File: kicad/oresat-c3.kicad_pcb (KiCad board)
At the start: 4 copper layers, 99.8 x 94.6 mm, 564 parts, among them J1 TFM-120-01-L-D-RA, J2 2-1734592-0, J3 733000020, J4 733000020, J5 DM3BT-DSF-PEJS, J6 Conn_01x02, Q1 NTR4101P, Q10 FDMQ86530L, Q11 DMP2240UDM-7, Q12 PMV45EN, Q2 NTR4101P, Q3 NTR4101P, Q4 PMV45EN, Q5 DMP2240UDM-7, Q6 MMBT2907, Q7 DMP2240UDM-7, Q8 FDMQ86530L, Q9 DMP2240UDM-7, U1 OSD3358-512M-BSM, U10 SN74AUC1G07DCKR, U11 RCLAMP0504FB, U12 RCLAMP0504FB, U13 MAX892LEUA+T, U14 TLVH431, U15 Qorvo 856930, U16 AX5043, U17 SI4112-GM, U18 LT5534, U19 BDCN-20-13+, U2 BP0805A1308, U20 QPC1022, U21 TQP7M9105, U22 LT5534, U23 AX5043, U24 RV-3028-C7, U25 SN74LVC1G11IDCKRQ1, U26 TLV7041DBV, U27 LP2985AIM5-1.8_NOPB, U28 TLV1704-SEP, U29 TQP3M9036, U3 BP0805A1308, U30 FM24CL64B-GTR, U31 LP2985AIM5-3.3, U32 SF2446E, U33 SF2446E, U34 TPS259621DDA, U35 TPS259620DDA, U36 LTC3624-5, U37 LTC4300A-1, U38 LP2985AIM5-3.3, U39 TCAN330, U4 BGB741L7ESD, U40 MAX941EUA+, U41 TQP3M9036, U42 LP2985AIM5-1.8_NOPB, U43 FSUSB42MUX, U5 BP0805A1308, U6 LTC3624-5, U7 MAC-24+, U8 TCAN330, U9 EMMC+RESET+5.1-COMPATIBLE-BA, X1 TYKTBLSANF-16.000000, X2 TYKTBLSANF-16.000000, Y1 ECS-240-12-30BQ-AEN-TR, Y2 ABS07-32.768KHZ-T

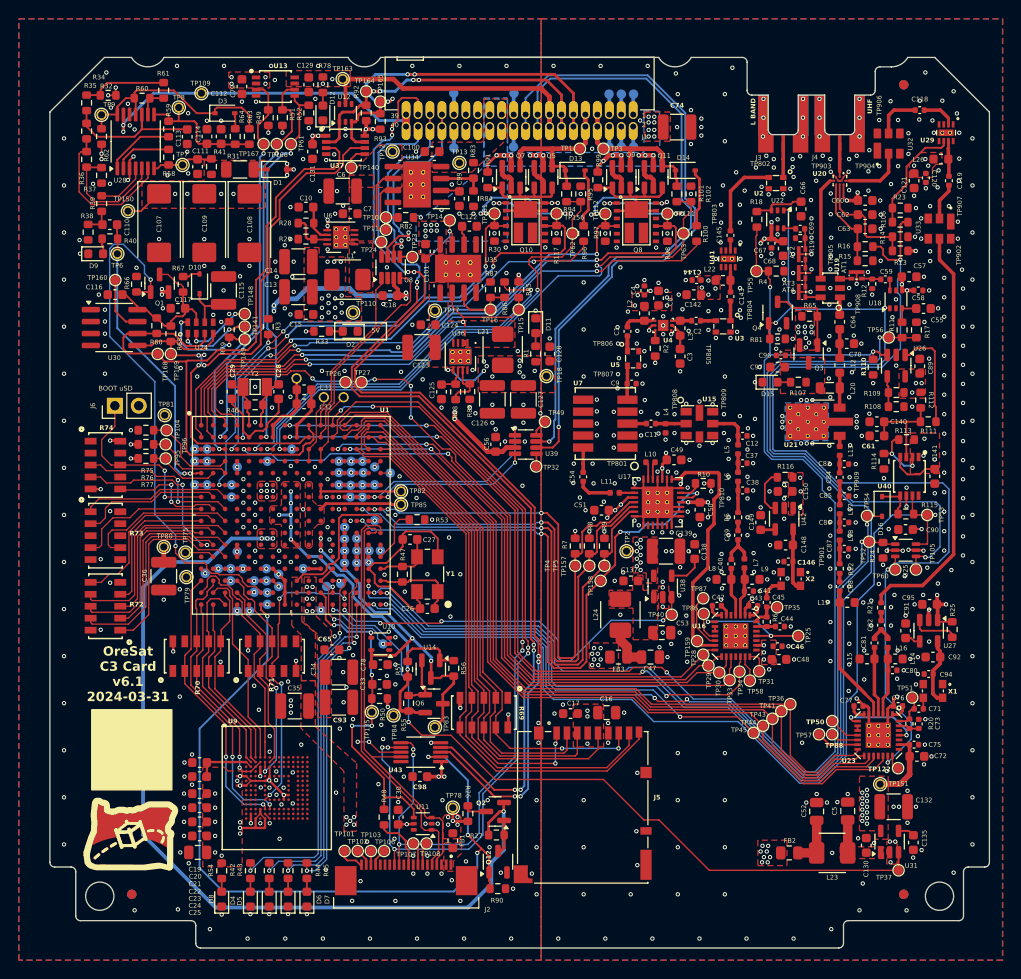
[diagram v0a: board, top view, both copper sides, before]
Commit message: C3 v6.1 release
Updated to KiCad 9.0.6. Updated to version 6.1; there are small changes that have been lost in time. Lots of new ERC and DRC errors that need to be cleaned up.
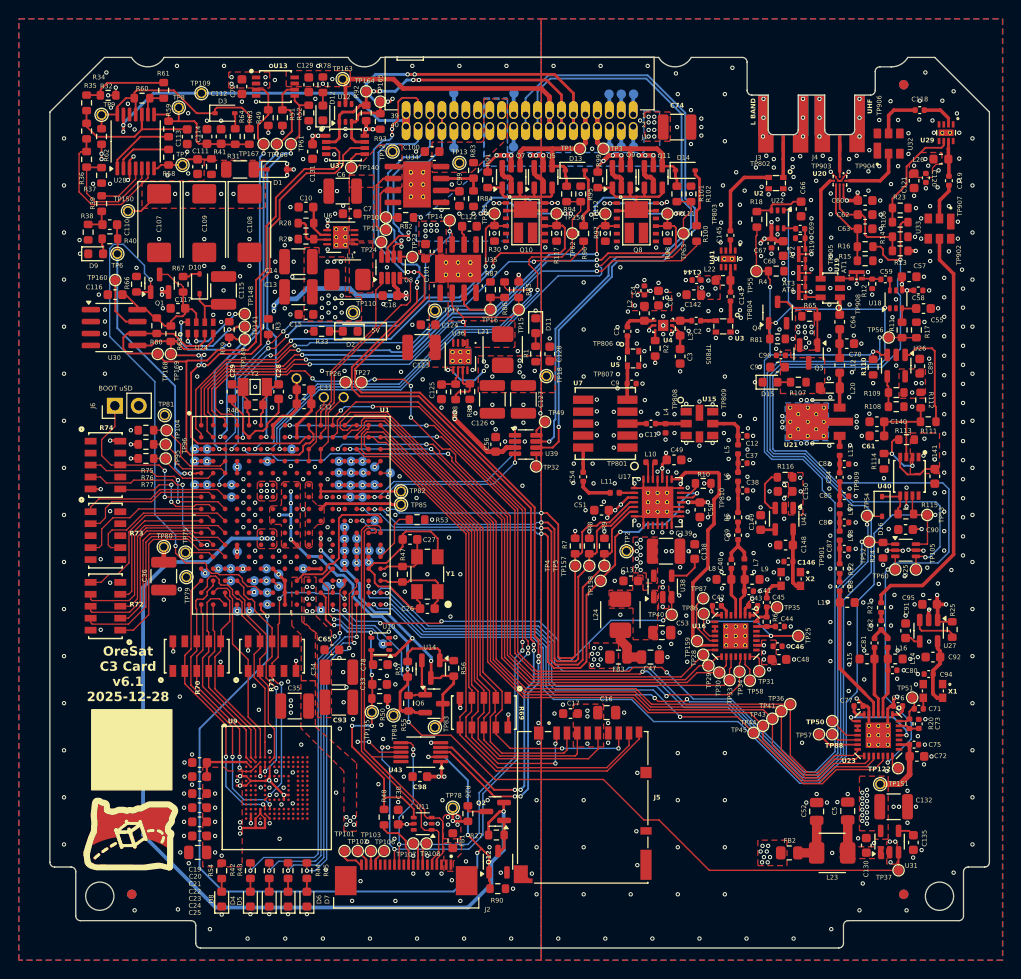
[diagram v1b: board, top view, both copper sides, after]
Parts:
- D15, D9: value GREEN -> AMBER
- U1: value OSD3358-512M-BSM -> OSD3358-1G-ISM
- U9: value EMMC+RESET+5.1-COMPATIBLE-BA -> SFEM016GB1EA1TO-I-GE-121-STD
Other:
- board text added: "OreSat C3 Card v${REVISION} ${ISSUE_DATE}"
- board text removed: "OreSat C3 Card v6.1 2024-03-31"
